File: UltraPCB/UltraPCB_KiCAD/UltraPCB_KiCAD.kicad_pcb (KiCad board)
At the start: 2 copper layers, 69 x 112.2 mm, 52 parts, among them J1 USB_C_Receptacle_PowerOnly_6P, J2 Conn_01x04_Pin, Q1 IRLML6401, Q2 IRLML6401, Q3 IRLML6401, Q4 IRLML6401, Q5 IRLML6401, Q6 IRLML6244, SW1 SW_Push, SW2 SW_Push, U2 LM3670MF, U3 LTC-4627JD, U4 STM32F030K6Tx

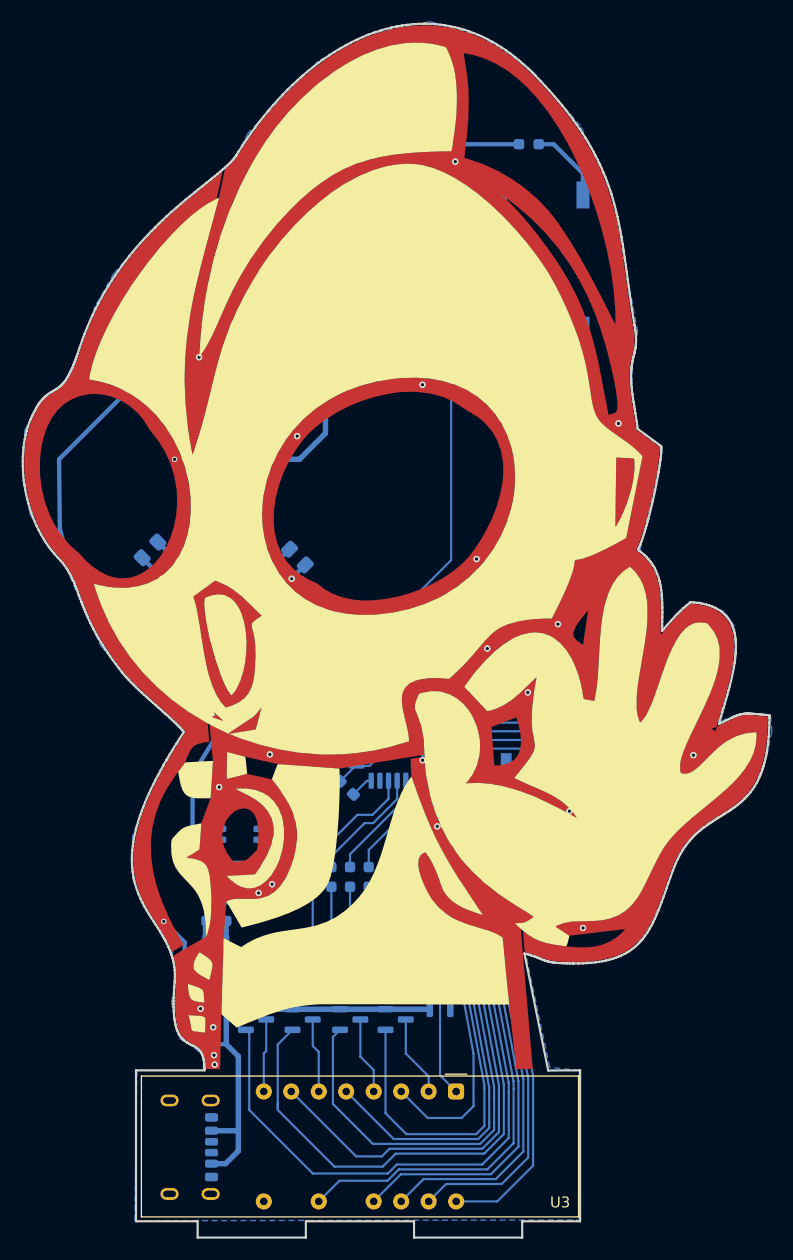
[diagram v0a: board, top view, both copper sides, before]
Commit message: New components
D1, SW1-2 changed. Mounting pads added. Minor improvements.
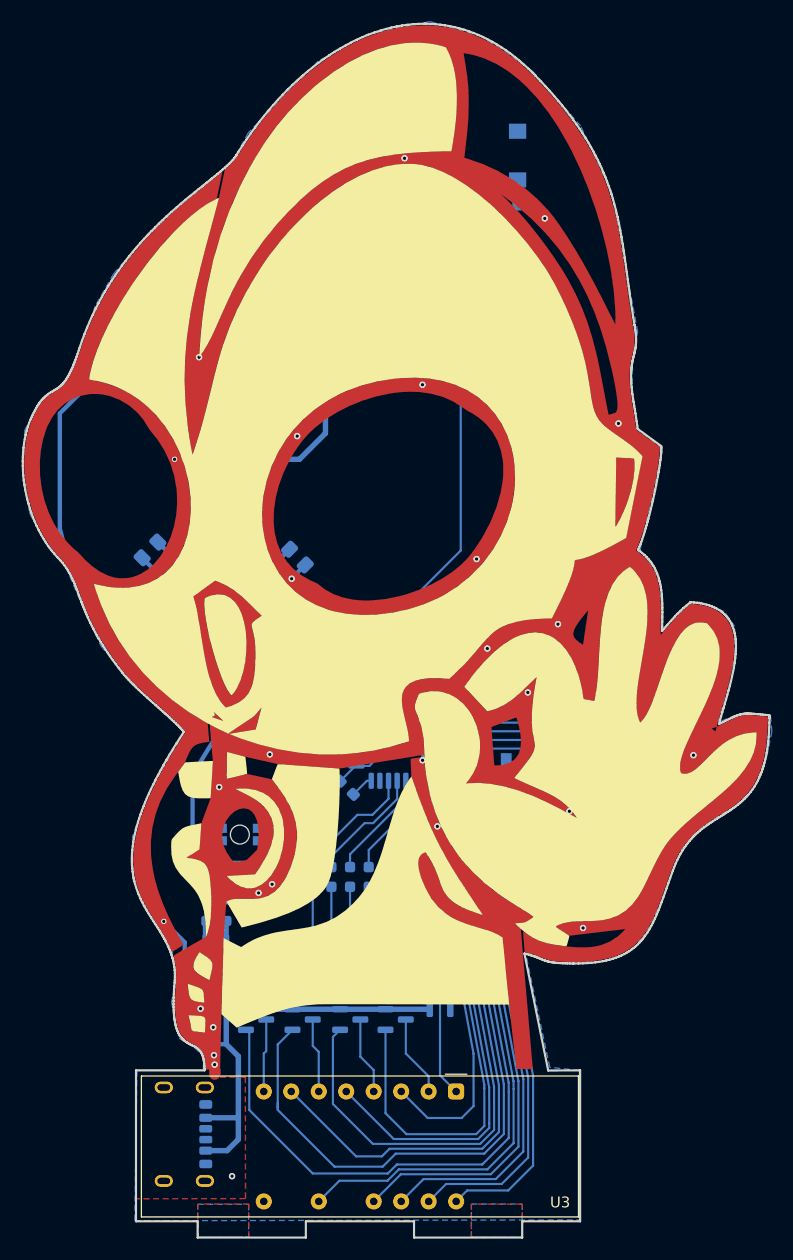
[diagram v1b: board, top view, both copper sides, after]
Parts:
- removed D1: LTST-C235KGKRKT, LED_SMD:LED_LiteOn_LTST-C235KGKRKT
- added D4: Red & Blue, 120°, Library:WL-SBRW_1205_reverse mount, B.Cu at (132.1, 123.2)
- SW1, SW2: footprint Button_Switch_SMD:SW_MEC_5GSH9 -> Button_Switch_SMD:SW_SPST_Omron_B3FS-100xP
- moved SW1 28.5 mm to (153.8, 60.5), turned to 0 degrees
- moved R13 21.8 mm to (156.9, 65.1), turned to 180 degrees
- moved R14 21.8 mm to (137.8, 65.0), turned to 0 degrees
- moved SW2 21.5 mm to (140.9, 60.5), turned to 0 degrees
- moved BZ1 2.31 mm to (144.2, 74.5)
- moved Q6 1.60 mm to (151.6, 78.7)
- moved J1 1.31 mm to (125.9, 150.9)
- moved R12 0.68 mm to (137.9, 119.5)
- moved R11 0.66 mm to (136.1, 119.5)
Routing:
- net /SW2_IN: track 7.19 -> 2.38 mm
- net +3V3: track 165.9 -> 162.1 mm
- net +5V: track 104.1 -> 101.0 mm
- net Net-(BZ1--): track 10.0 -> 12.6 mm
- net /SW1_IN: track 4.62 -> 2.34 mm
- net /Timer3_PWM: track 33.7 -> 32.7 mm
- net GND: track 12.9 -> 13.8 mm, vias 21 -> 23
- net /LED_Red: track 8.55 -> 9.25 mm
- net /LED_Blue: track 6.38 -> 6.95 mm
- added copper zone on B.Cu, net (none)
- added copper zone on F.Cu, net (none)
- added copper zone on F.Cu, net GND
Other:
- board text added: "3V3"
- board text added: "5V USB"
- board text added: "A"
- board text added: "B"
- board text added: "CLK"
- board text added: "GND"
- board text added: "SWD"

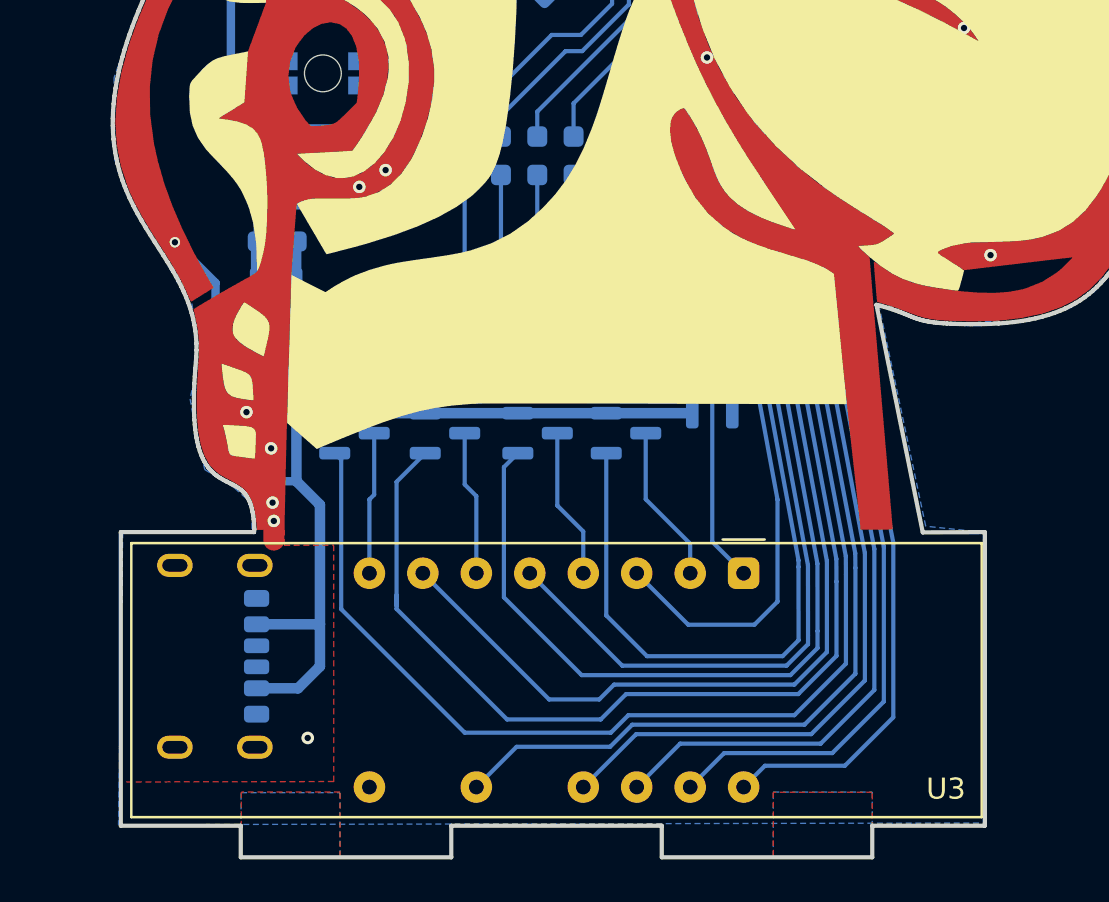
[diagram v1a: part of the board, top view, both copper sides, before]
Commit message: Production ready v1.0
Added production files. Components now have mouser part numbers. 7seg display was upside down so it was corrected. All production ready.
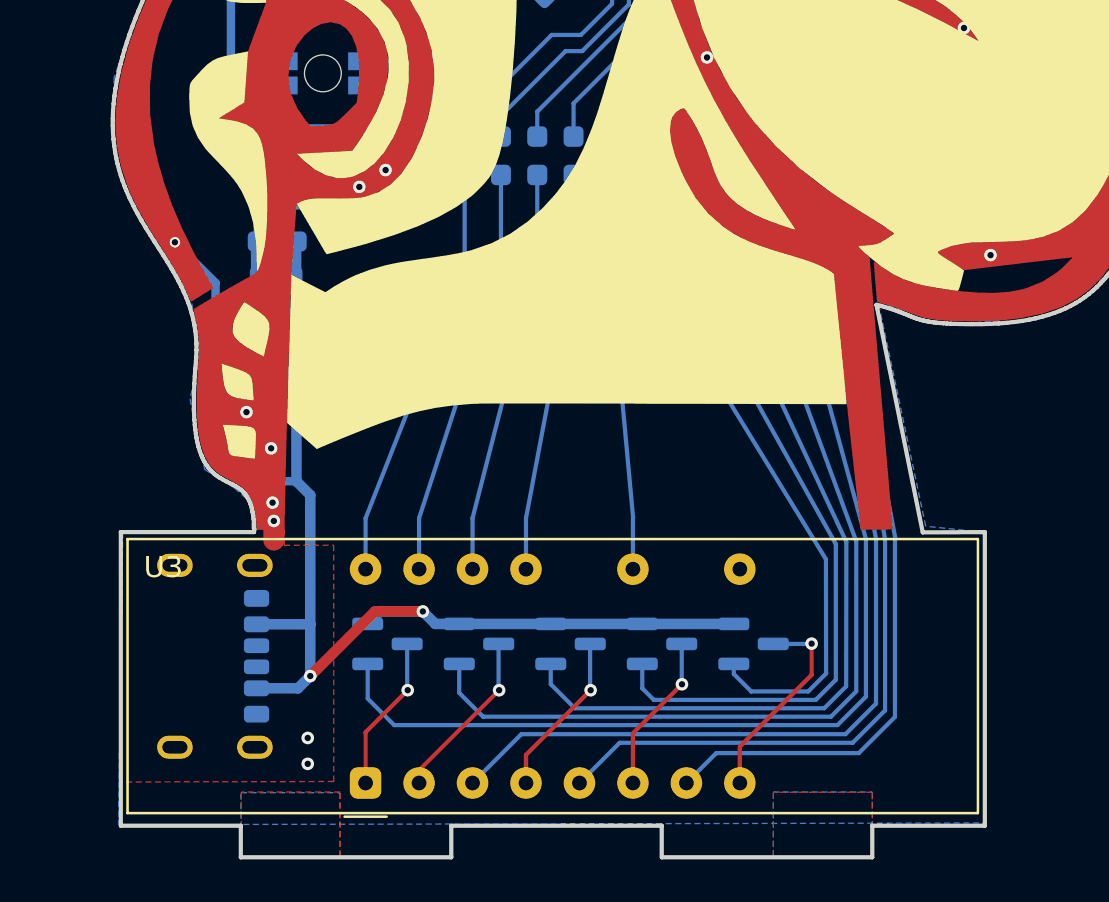
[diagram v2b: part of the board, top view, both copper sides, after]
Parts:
- U2: value LM3670MF -> LM3670MF-3.3
- moved Q4 21.4 mm to (152.6, 150.3)
- moved R2 20.7 mm to (138.8, 127.1)
- moved U3 20.5 mm to (134.1, 156.9), turned to 90 degrees
- moved Q1 19.5 mm to (135.2, 150.3), turned to 0 degrees
- moved R7 17.2 mm to (140.6, 127.1)
- moved R15 15.5 mm to (154.4, 127.1)
- moved R4 15.5 mm to (156.1, 127.1)
- moved Q3 14.4 mm to (148.2, 150.3)
- moved R1 13.8 mm to (142.3, 127.1)
- moved R5 13.8 mm to (157.8, 127.1)
- moved Q2 12.2 mm to (139.5, 150.3)
- moved R8 12.1 mm to (159.5, 127.1)
- moved R3 10.4 mm to (144.0, 127.1)
- moved R16 10.3 mm to (152.6, 127.1)
- moved Q5 10.1 mm to (143.9, 150.3)
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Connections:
- U4 pad 14: /DispB -> /DispDP
- U4 pad 15: /DispG -> /DispE
- U4 pad 18: /DispA -> /DispD
- U4 pad 19: /DispC -> /Display1
- U4 pad 20: /DispF -> /Display2
- U4 pad 21: /Display4 -> /DisplayL
- U4 pad 25: /DispDP -> /Display4
- U4 pad 26: /DisplayL -> /DispF
- U4 pad 27: /DispE -> /DispC
- U4 pad 28: /Display2 -> /DispA
- U4 pad 29: /DispD -> /DispG
- U4 pad 30: /Display1 -> /DispB
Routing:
- net /DispDP: track 8.96 -> 49.5 mm
- net /DispB: track 49.5 -> 11.7 mm
- net /DispE: track 9.72 -> 46.9 mm
- net /DispG: track 46.9 -> 11.0 mm
- net Net-(Q1-G): track 21.7 -> 51.7 mm
- net Net-(Q4-G): track 60.2 -> 31.7 mm
- net /Display4: track 37.4 -> 8.96 mm
- net /DispF: track 37.7 -> 9.34 mm
- net /DisplayL: track 9.34 -> 37.4 mm
- net /DispC: track 37.6 -> 9.72 mm
- net /DispA: track 38.0 -> 10.1 mm
- net /Display2: track 10.1 -> 37.7 mm
- net /DispD: track 11.0 -> 38.0 mm
- net Net-(U3-F): track 45.1 -> 18.8 mm
- net /Display1: track 11.7 -> 37.6 mm
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
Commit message: Rev. 1.1
Error correction and new folder structure for production files
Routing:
- net GND: track 13.8 -> 325.6 mm
- net +5V: track 105.7 -> 161.0 mm
- net +3V3: track 162.1 -> 168.6 mm
- net Net-(U3-E): track 39.9 -> 41.8 mm
- net Net-(U3-D): track 44.2 -> 45.9 mm
- net Net-(U3-DP): track 38.2 -> 37.7 mm
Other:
- outline, holes or cut-outs redrawn
- board text added: "UltraTimer rev. 1.1"
- board text removed: "UltraTimer rev. 1.0"

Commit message: Revision 1.2
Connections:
- U4 pad 11: unconnected-(U4-PA5-Pad11) -> /SW2_IN
- U4 pad 13: unconnected-(U4-PA7-Pad13) -> /SW1_IN
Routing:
- net /SW2_IN: track 2.38 -> 82.6 mm
- net /SW1_IN: track 2.34 -> 55.8 mm
- net GND: track 325.6 -> 337.0 mm
- net +3V3: track 168.6 -> 174.0 mm
- net +5V: track 161.0 -> 156.5 mm
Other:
- board text added: "2025"
- board text added: "UltraTimer rev. 1.2"
- board text removed: "2024"
- board text removed: "UltraTimer rev. 1.1"

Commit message: Q1-5 replaced
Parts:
- Q1, Q2, Q3, Q4, Q5: value IRLML6401 -> SQ2325ES-T1_GE3
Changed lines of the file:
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@@
 	(title_block
 		(title "UltraPCB")
-		(date "2025-02-13")
+		(date "2025-03-02")
 		(rev "1.2")
 		(comment 1 "All units in mm")
@@
 			(outputformat 4)
 			(mirror no)
-			(drillshape 0)
+			(drillshape 2)
 			(scaleselection 1)
 			(outputdirectory "production/UltraPCB_gerber/")
@@
 			)
 		)
-		(property "Value" "IRLML6401"
+		(property "Value" "SQ2325ES-T1_GE3"
 			(at 0 -2.4 0)
 			(layer "B.Fab")
@@
 			)
 		)
-		(property "Datasheet" "https://www.infineon.com/dgdl/irlml6401pbf.pdf?fileId=5546d462533600a401535668b96d2634"
+		(property "Datasheet" "https://www.vishay.com/docs/67847/sq2325es.pdf"
 			(at 0 0 180)
 			(unlocked yes)
@@
 			)
 		)
-		(property "Description" "-4.3A Id, -12V Vds, 50mOhm Rds, P-Channel HEXFET Power MOSFET, SOT-23"
+		(property "Description" "MOSFET, P-Chnl, 150-V (D-S), V GS(th) -2.5V to -3.5V, AEC-Q101 Qualified, SOT-23"
 			(at 0 0 180)
 			(unlocked yes)
@@
 			)
 		)
-		(property "SupplierPartNumber1" " 942-IRLML6401TRPBF "
+		(property "SupplierPartNumber1" " 78-SQ2325ES-T1_GE3"
 			(at 0 0 0)
 			(unlocked yes)
@@
 			)
 		)
-		(property "Value" "IRLML6401"
+		(property "Value" "SQ2325ES-T1_GE3"
 			(at 0 -2.4 0)
 			(layer "B.Fab")
@@
 			)
 		)
-		(property "Datasheet" "https://www.infineon.com/dgdl/irlml6401pbf.pdf?fileId=5546d462533600a401535668b96d2634"
+		(property "Datasheet" "https://www.vishay.com/docs/67847/sq2325es.pdf"
 			(at 0 0 180)
 			(unlocked yes)
@@
 			)
 		)
-		(property "Description" "-4.3A Id, -12V Vds, 50mOhm Rds, P-Channel HEXFET Power MOSFET, SOT-23"
+		(property "Description" "MOSFET, P-Chnl, 150-V (D-S), V GS(th) -2.5V to -3.5V, AEC-Q101 Qualified, SOT-23"
 			(at 0 0 180)
 			(unlocked yes)
@@
 			)
 		)
-		(property "SupplierPartNumber1" " 942-IRLML6401TRPBF "
+		(property "SupplierPartNumber1" " 78-SQ2325ES-T1_GE3"
 			(at 0 0 0)
 			(unlocked yes)
@@
 			)
 		)
-		(property "Value" "IRLML6401"
+		(property "Value" "SQ2325ES-T1_GE3"
 			(at 0 -2.4 0)
 			(layer "B.Fab")
@@
 			)
 		)
-		(property "Datasheet" "https://www.infineon.com/dgdl/irlml6401pbf.pdf?fileId=5546d462533600a401535668b96d2634"
+		(property "Datasheet" "https://www.vishay.com/docs/67847/sq2325es.pdf"
 			(at 0 0 180)
 			(unlocked yes)
@@
 			)
 		)
-		(property "Description" "-4.3A Id, -12V Vds, 50mOhm Rds, P-Channel HEXFET Power MOSFET, SOT-23"
+		(property "Description" "MOSFET, P-Chnl, 150-V (D-S), V GS(th) -2.5V to -3.5V, AEC-Q101 Qualified, SOT-23"
 			(at 0 0 180)
 			(unlocked yes)
@@
 			)
 		)
-		(property "SupplierPartNumber1" " 942-IRLML6401TRPBF "
+		(property "SupplierPartNumber1" " 78-SQ2325ES-T1_GE3"
 			(at 0 0 0)
 			(unlocked yes)
@@
 			)
 		)
-		(property "Value" "IRLML6401"
+		(property "Value" "SQ2325ES-T1_GE3"
 			(at 0 -2.4 0)
 			(layer "B.Fab")
@@
 			)
 		)
-		(property "Datasheet" "https://www.infineon.com/dgdl/irlml6401pbf.pdf?fileId=5546d462533600a401535668b96d2634"
+		(property "Datasheet" "https://www.vishay.com/docs/67847/sq2325es.pdf"
 			(at 0 0 180)
 			(unlocked yes)
@@
 			)
 		)
-		(property "Description" "-4.3A Id, -12V Vds, 50mOhm Rds, P-Channel HEXFET Power MOSFET, SOT-23"
+		(property "Description" "MOSFET, P-Chnl, 150-V (D-S), V GS(th) -2.5V to -3.5V, AEC-Q101 Qualified, SOT-23"
 			(at 0 0 180)
 			(unlocked yes)
@@
 			)
 		)
-		(property "SupplierPartNumber1" " 942-IRLML6401TRPBF "
+		(property "SupplierPartNumber1" " 78-SQ2325ES-T1_GE3"
 			(at 0 0 0)
 			(unlocked yes)
@@
 			)
 		)
-		(property "Value" "IRLML6401"
+		(property "Value" "SQ2325ES-T1_GE3"
 			(at 0 -2.4 0)
 			(layer "B.Fab")
@@
 			)
 		)
-		(property "Datasheet" "https://www.infineon.com/dgdl/irlml6401pbf.pdf?fileId=5546d462533600a401535668b96d2634"
+		(property "Datasheet" "https://www.vishay.com/docs/67847/sq2325es.pdf"
 			(at 0 0 180)
 			(unlocked yes)
@@
 			)
 		)
-		(property "Description" "-4.3A Id, -12V Vds, 50mOhm Rds, P-Channel HEXFET Power MOSFET, SOT-23"
+		(property "Description" "MOSFET, P-Chnl, 150-V (D-S), V GS(th) -2.5V to -3.5V, AEC-Q101 Qualified, SOT-23"
 			(at 0 0 180)
 			(unlocked yes)
@@
 			)
 		)
-		(property "SupplierPartNumber1" " 942-IRLML6401TRPBF "
+		(property "SupplierPartNumber1" " 78-SQ2325ES-T1_GE3"
 			(at 0 0 0)
 			(unlocked yes)

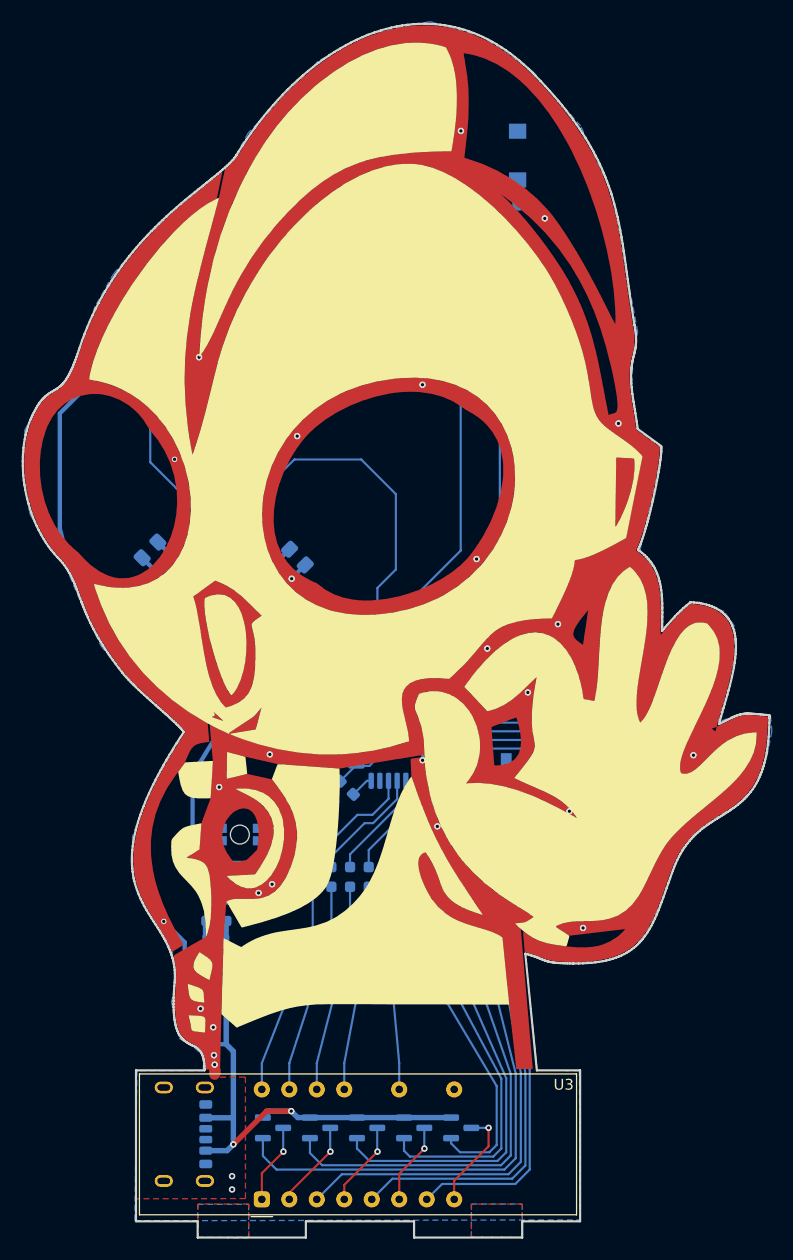
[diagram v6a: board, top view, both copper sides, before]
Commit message: Changed to KiCAD 9 and rounded all tracks
Plugin Round Tracks was used for automatically rounding all tracks
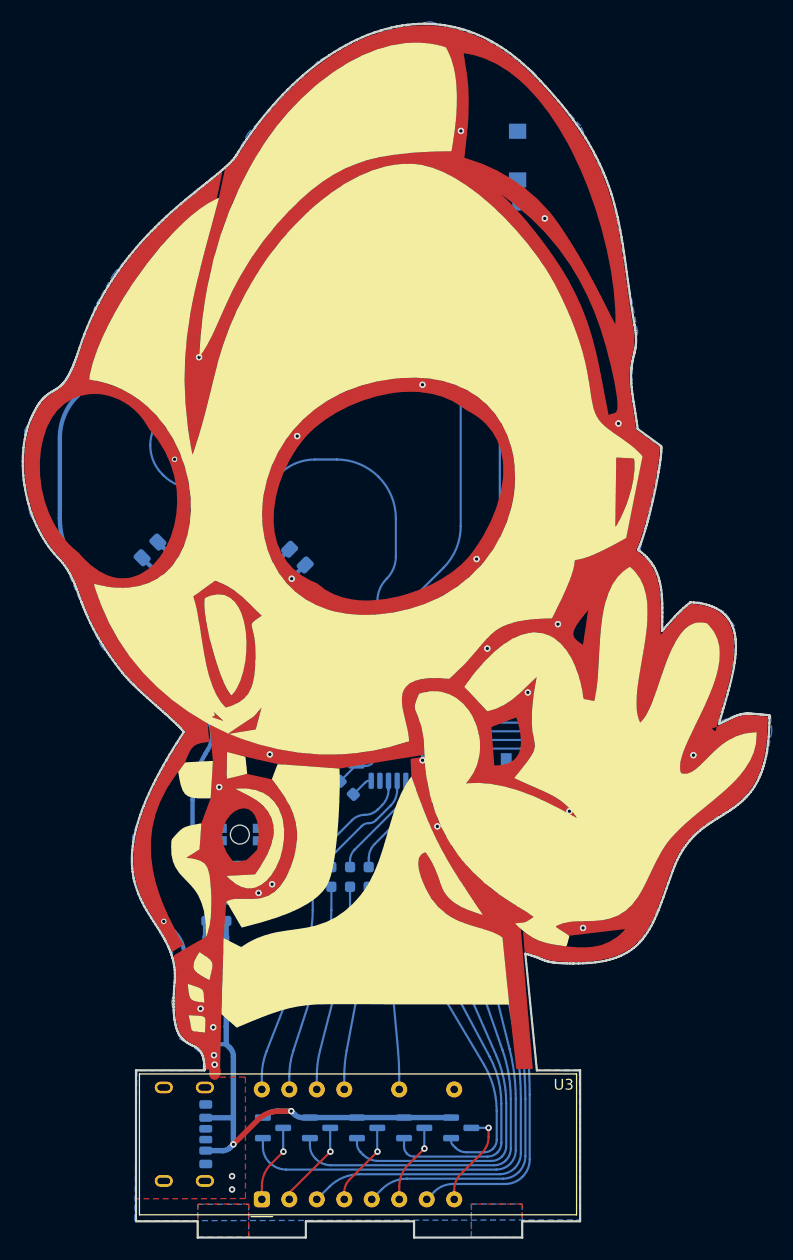
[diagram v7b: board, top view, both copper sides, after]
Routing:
- net GND: track 337.0 -> 325.4 mm
- net +5V: track 156.5 -> 153.1 mm
- net +3V3: track 174.0 -> 170.7 mm
- net /SW2_IN: track 82.6 -> 80.5 mm
- net /DispDP: track 49.5 -> 48.0 mm
- net /DispE: track 46.9 -> 45.4 mm
- net /Display1: track 37.6 -> 36.5 mm
- net /DispD: track 38.0 -> 36.9 mm
- net /Display2: track 37.7 -> 36.6 mm
- net /DisplayL: track 37.4 -> 36.4 mm
- net /Display3: track 37.1 -> 36.1 mm
- net /SW1_IN: track 55.8 -> 54.9 mm
- net Net-(U3-DP): track 37.7 -> 37.1 mm
- net Net-(U3-E): track 41.8 -> 41.2 mm
- net /Timer3_PWM: track 32.7 -> 32.2 mm
